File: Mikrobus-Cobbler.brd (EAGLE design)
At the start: 62.2 x 45.7 mm, 2 parts

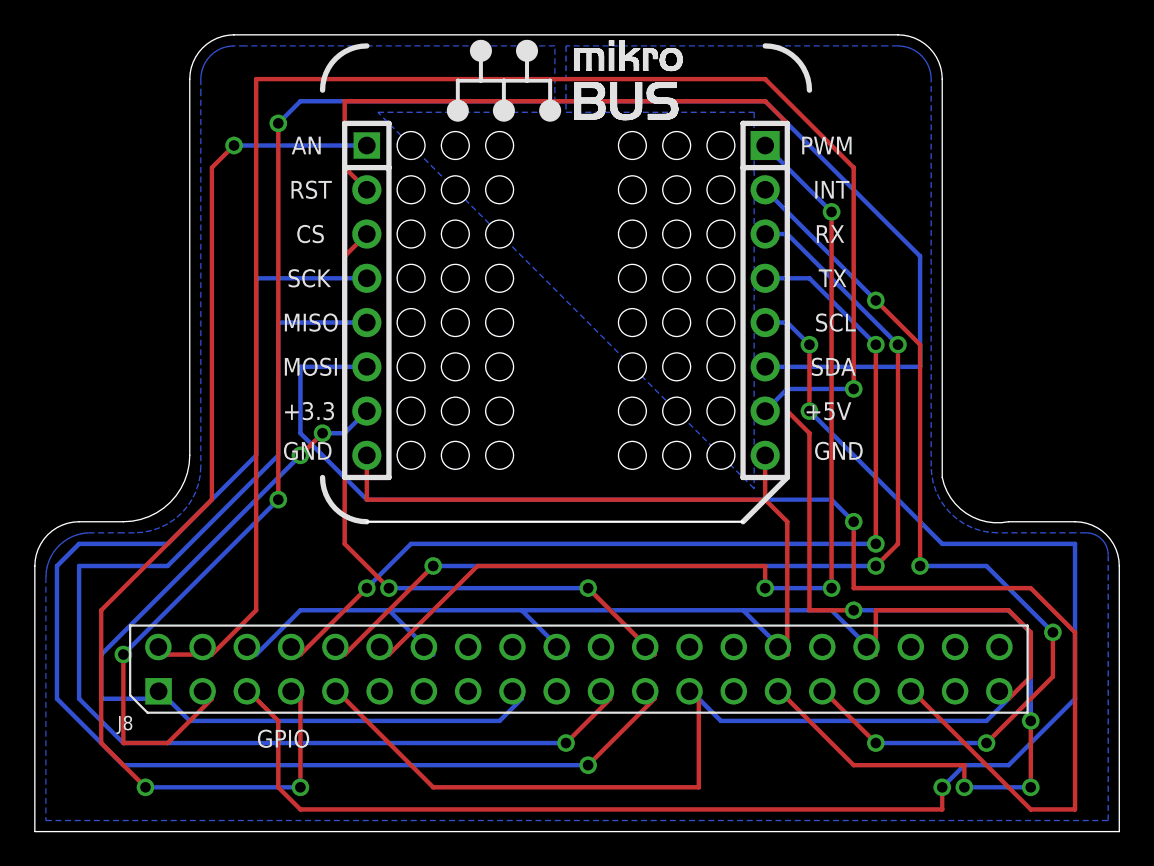
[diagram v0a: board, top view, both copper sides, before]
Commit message: Changed back to rectangle hole as Fab says yes it can do
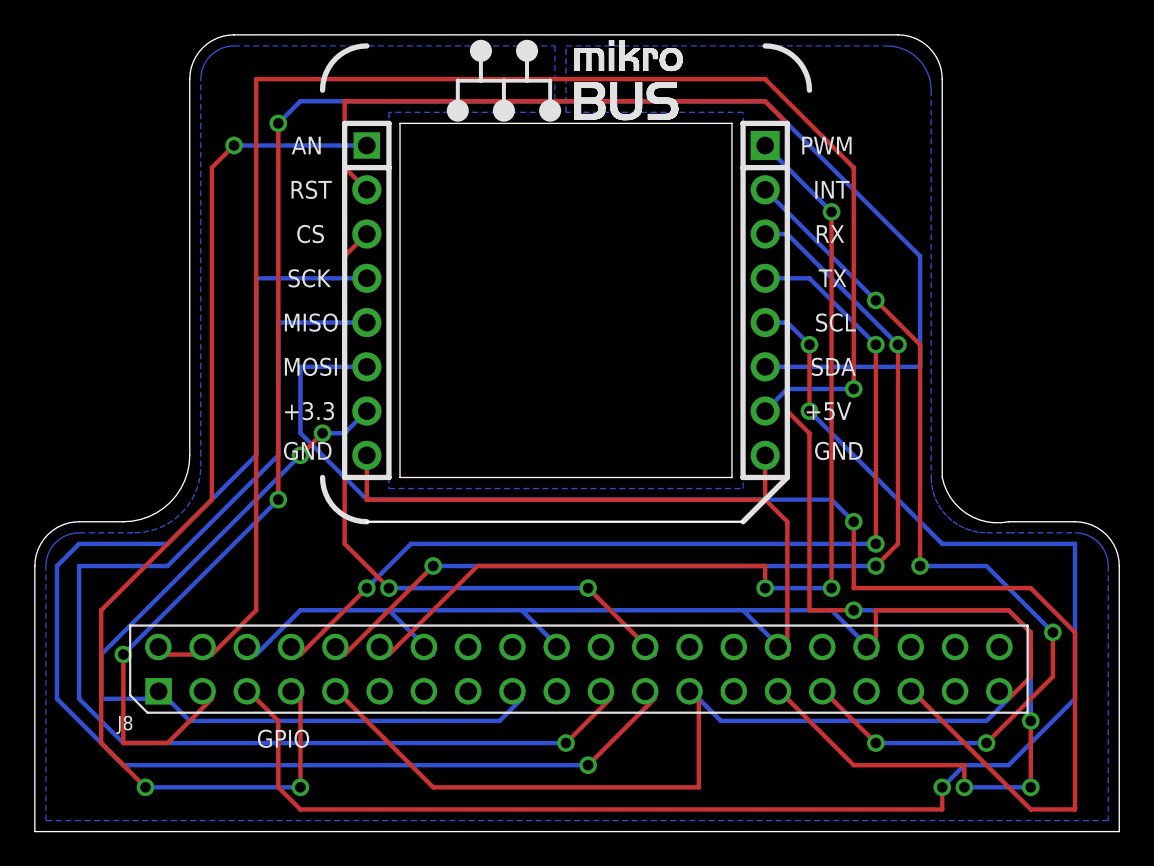
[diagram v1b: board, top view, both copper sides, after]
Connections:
- net N$10 renamed PWM
- net N$11 renamed INT
- net N$12 renamed RX
- net N$13 renamed TX
- net N$14 renamed SCL
- net N$15 renamed SDA
- net N$2 renamed +5V
- net N$3 renamed +3.3V
- net N$4 renamed AN
- net N$5 renamed RST
- net N$6 renamed SCK
- net N$7 renamed CS
- net N$8 renamed MISO
- net N$9 renamed MOSI
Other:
- outline, holes or cut-outs redrawn
